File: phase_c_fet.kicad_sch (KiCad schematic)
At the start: 24 parts, among them Q18 IAUS300N08S5N0, Q19 IAUS300N08S5N0, Q20 IAUS300N08S5N0, Q21 IAUS300N08S5N0, U11 INA241A2

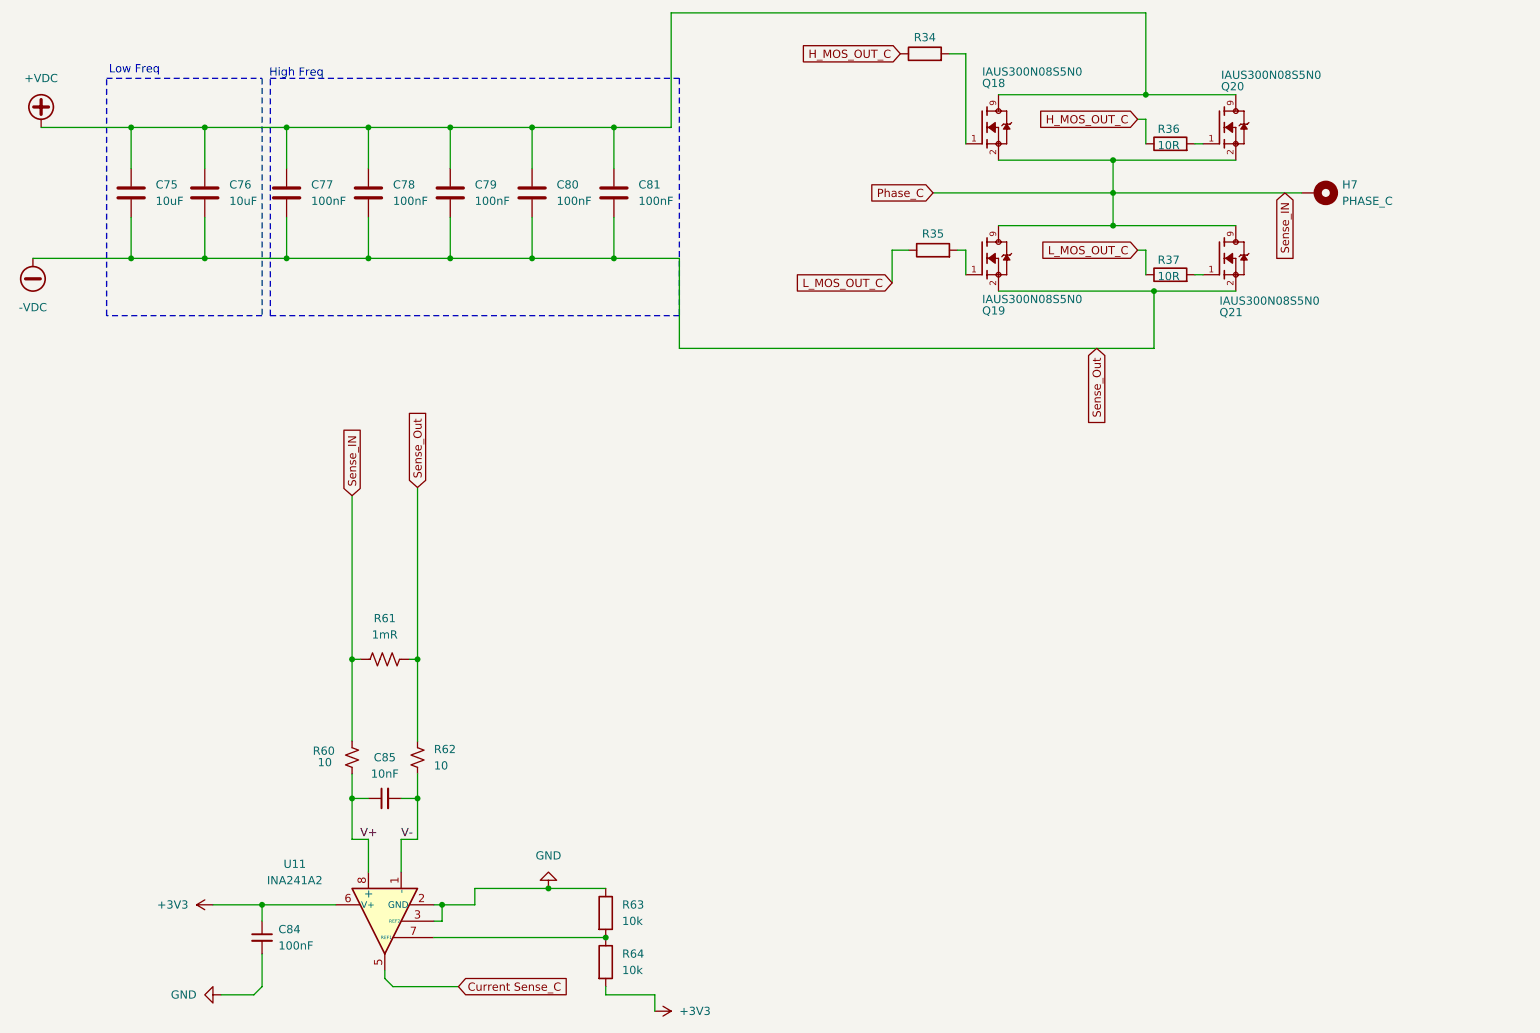
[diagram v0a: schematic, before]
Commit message: update: revised label
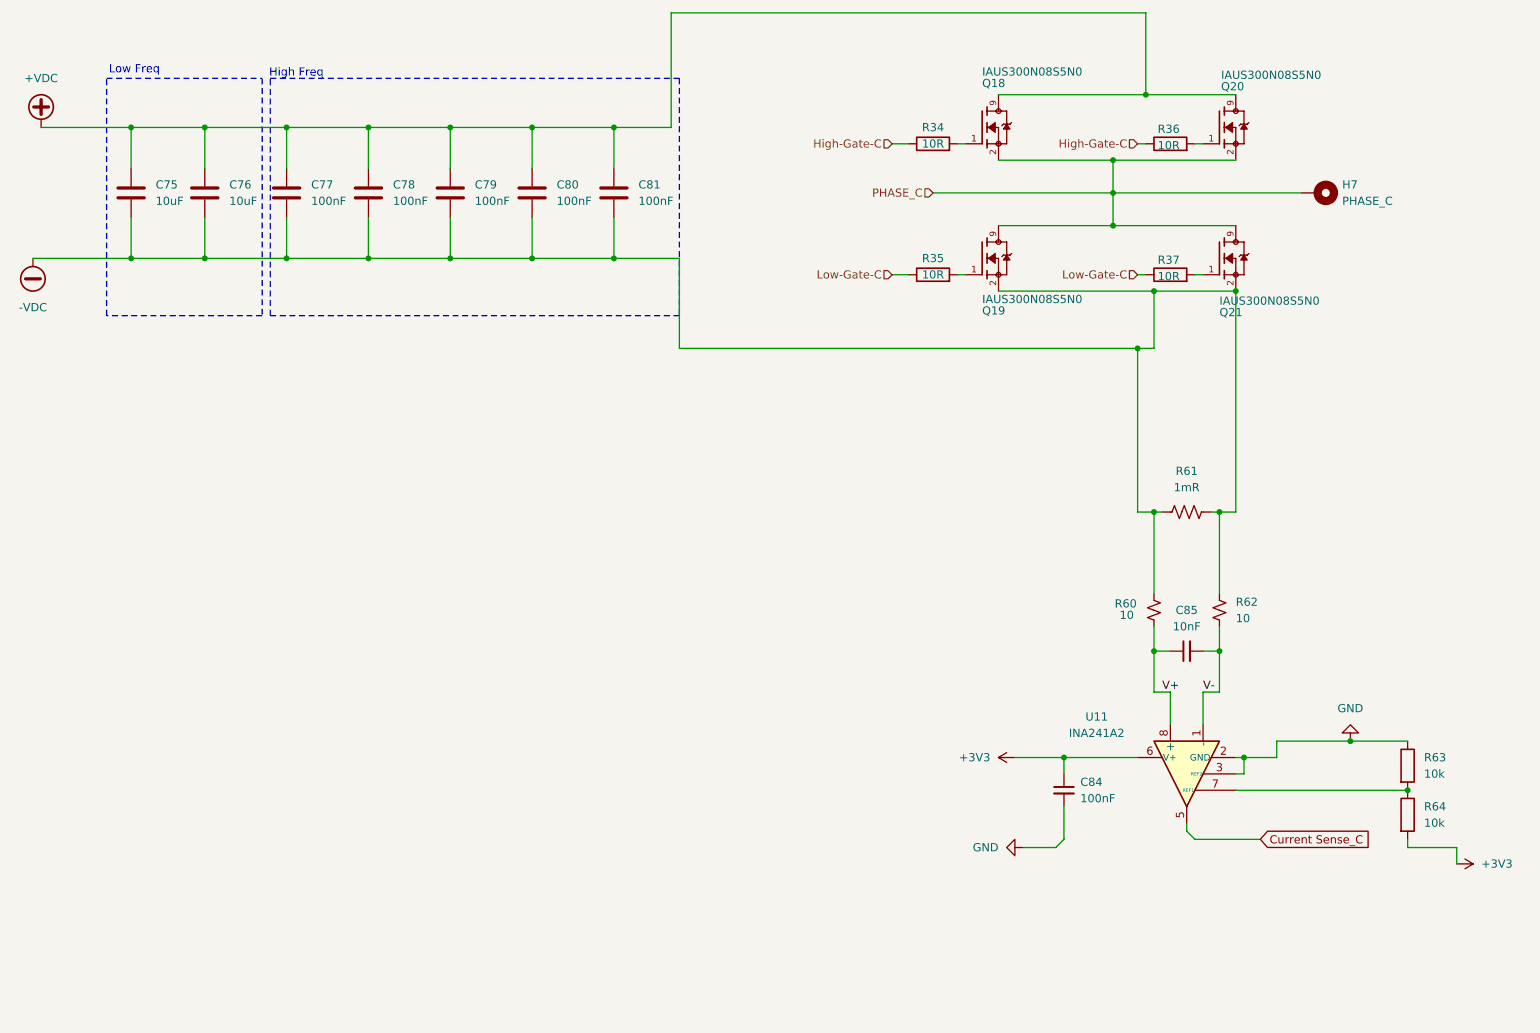
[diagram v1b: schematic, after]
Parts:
- C84, C85: footprint OpenMD:C_0402_1005Metric -> Capacitor_SMD:C_0402_1005Metric_Pad0.74x0.62mm_HandSolder
- R60, R62: footprint OpenMD:R_0402_1005Metric -> Resistor_SMD:R_0402_1005Metric_Pad0.72x0.64mm_HandSolder
- R61: footprint OpenMD:R_2512_6332Metric -> Resistor_SMD:R_2512_6332Metric_Pad1.40x3.35mm_HandSolder
- R63, R64: footprint (none) -> Resistor_SMD:R_1812_4532Metric_Pad1.30x3.40mm_HandSolder
- U11: footprint OpenMD:SOT-23-8 -> Package_TO_SOT_SMD:SOT-23-8_Handsoldering
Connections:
- net -VDC: now also R60.1, R61.1
- net H_MOS_OUT_C renamed High-Gate-C
- net L_MOS_OUT_C renamed Low-Gate-C
- net Phase_C renamed PHASE_C
- net PHASE_C: no longer R60.1, R61.1
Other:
- moved on the sheet: C84, C85, R34, R35, R60, R61, R62, R63, R64, U11

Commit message: LAST I HOPE
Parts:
- added R72: 1mR, Resistor_SMD:R_2512_6332Metric_Pad1.40x3.35mm_HandSolder, symbol OpenMD:R_US
- R63, R64: footprint Resistor_SMD:R_1812_4532Metric_Pad1.30x3.40mm_HandSolder -> Resistor_SMD:R_0603_1608Metric_Pad0.98x0.95mm_HandSolder
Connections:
- net -VDC: now also R72.1, R72.2
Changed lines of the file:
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@@
 	)
 	(junction
+		(at 205.74 113.03)
+		(diameter 0)
+		(color 0 0 0 0)
+	)
+	(junction
 		(at 121.92 67.31)
 		(diameter 0)
@@
 	)
 	(junction
+		(at 215.9 113.03)
+		(diameter 0)
+		(color 0 0 0 0)
+	)
+	(junction
 		(at 109.22 67.31)
 		(diameter 0)
@@
 	(wire
 		(pts
+			(xy 215.9 113.03) (xy 215.9 119.38)
+		)
+		(stroke
+			(width 0)
+			(type default)
+		)
+	)
+	(wire
+		(pts
 			(xy 212.09 49.53) (xy 213.36 49.53)
 		)
@@
 	(wire
 		(pts
-			(xy 215.9 106.68) (xy 215.9 119.38)
+			(xy 205.74 113.03) (xy 205.74 119.38)
+		)
+		(stroke
+			(width 0)
+			(type default)
+		)
+	)
+	(wire
+		(pts
+			(xy 215.9 106.68) (xy 215.9 113.03)
 		)
 		(stroke
@@
 	(wire
 		(pts
-			(xy 205.74 106.68) (xy 205.74 119.38)
+			(xy 205.74 106.68) (xy 205.74 113.03)
 		)
 		(stroke
@@
 	(wire
 		(pts
+			(xy 214.63 113.03) (xy 215.9 113.03)
+		)
+		(stroke
+			(width 0)
+			(type default)
+		)
+	)
+	(wire
+		(pts
 			(xy 121.92 67.31) (xy 132.08 67.31)
 		)
@@
 	(wire
 		(pts
+			(xy 205.74 113.03) (xy 207.01 113.03)
+		)
+		(stroke
+			(width 0)
+			(type default)
+		)
+	)
+	(wire
+		(pts
 			(xy 71.12 67.31) (xy 83.82 67.31)
 		)
@@
 	)
 	(symbol
+		(lib_id "OpenMD:R_US")
+		(at 210.82 113.03 90)
+		(unit 1)
+		(exclude_from_sim no)
+		(in_bom yes)
+		(on_board yes)
+		(dnp no)
+		(fields_autoplaced yes)
+		(property "Reference" "R72"
+			(at 210.82 106.68 90)
+			(effects
+				(font
+					(size 1.27 1.27)
+				)
+			)
+		)
+		(property "Value" "1mR"
+			(at 210.82 109.22 90)
+			(effects
+				(font
+					(size 1.27 1.27)
+				)
+			)
+		)
+		(property "Footprint" "Resistor_SMD:R_2512_6332Metric_Pad1.40x3.35mm_HandSolder"
+			(at 211.074 112.014 90)
+			(effects
+				(font
+					(size 1.27 1.27)
+				)
+				(hide yes)
+			)
+		)
+		(property "Datasheet" "~"
+			(at 210.82 113.03 0)
+			(effects
+				(font
+					(size 1.27 1.27)
+				)
+				(hide yes)
+			)
+		)
+		(property "Description" "Resistor, US symbol"
+			(at 210.82 113.03 0)
+			(effects
+				(font
+					(size 1.27 1.27)
+				)
+				(hide yes)
+			)
+		)
+		(property "Rating" "3W"
+			(at 210.82 113.03 0)
+			(effects
+				(font
+					(size 1.27 1.27)
+				)
+				(hide yes)
+			)
+		)
+		(property "Source" "LCSC"
+			(at 210.82 113.03 0)
+			(effects
+				(font
+					(size 1.27 1.27)
+				)
+				(hide yes)
+			)
+		)
+		(property "Manufacturer_Part_Number" "ASR-M-3-0.5F"
+			(at 210.82 113.03 0)
+			(effects
+				(font
+					(size 1.27 1.27)
+				)
+				(hide yes)
+			)
+		)
+		(pin "2"
+		)
+		(pin "1"
+		)
+		(instances
+			(project "Motor_Driver_Shell_Eco"
+				(path "/63ef3b9c-05f1-4b00-812a-fede2372efc7/7c8dbef5-e40c-461c-862c-3f756f947d60/44c201c1-7b77-4d71-9df0-e81a0e74ce01"
+					(reference "R72")
+					(unit 1)
+				)
+			)
+		)
+	)
+	(symbol
 		(lib_id "OpenMD:C_Small")
 		(at 191.77 149.86 0)
@@
 			)
 		)
-		(property "Footprint" "Resistor_SMD:R_1812_4532Metric_Pad1.30x3.40mm_HandSolder"
+		(property "Footprint" "Resistor_SMD:R_0603_1608Metric_Pad0.98x0.95mm_HandSolder"
 			(at 243.332 146.05 90)
 			(effects
@@
 			)
 		)
-		(property "Footprint" "Resistor_SMD:R_1812_4532Metric_Pad1.30x3.40mm_HandSolder"
+		(property "Footprint" "Resistor_SMD:R_0603_1608Metric_Pad0.98x0.95mm_HandSolder"
 			(at 243.332 153.67 90)
 			(effects

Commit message: bit artık
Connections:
- net Current Sense_C renamed Current_Sense_C
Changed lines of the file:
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@@
 		)
 	)
-	(global_label "Current Sense_C"
+	(global_label "Current_Sense_C"
 		(shape input)
 		(at 222.25 157.48 0)

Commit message: rev3
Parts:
- removed H7: PHASE_C, MountingHole:MountingHole_3.7mm_Pad_Via, symbol Mechanical:MountingHole_Pad
- added MP3: Phase_A, WP-BUTR:WP-BUTR_7460307, symbol WP-BUTR:WP-BUTR
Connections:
- net GND is gone; now on net -VDC: C84.2, R63.1, U11.2 (GND), U11.3 (REF2), U11.4 (GND)
- net -VDC: no longer Q19.2, Q19.3, Q19.4, Q19.5, Q19.6, Q19.7, Q19.8, Q21.2, Q21.3, Q21.4, Q21.5, Q21.6, Q21.7, Q21.8, R61.2, R62.1, R72.2
- net PHASE_C: now also MP3.1, MP3.2, MP3.3, MP3.4, MP3.5, MP3.6, MP3.7, MP3.8
- net +3V3 renamed +3V3F
- new net: Q19.2, Q19.3, Q19.4, Q19.5, Q19.6, Q19.7, Q19.8, Q21.2, Q21.3, Q21.4, Q21.5, Q21.6, Q21.7, Q21.8, R61.2, R62.1, R72.2
